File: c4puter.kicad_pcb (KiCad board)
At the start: 6 copper layers, 200 x 200 mm, 181 parts, among them J1 PDI, J7 19V 3A, J8 DEBUG, Q1 AOD4189, Q2 AOD4189, Q3 2N7002, U1 ATXMEGA8E5-MU

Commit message: MOAR WORK
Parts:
- added C9: 100n, IPC7351-Nominal:CAPC1005X55, F.Cu at (90.5, 1.96)
- added J2: MICROSD, manuf:AMPHENOL-114-00841-68, F.Cu at (100.0, 4.00)
- added R56: 100k, IPC7351-Nominal:RESC1608X50, F.Cu at (90.5, 3.77)
- LIMB1: value LPC435xFET256 -> ATSAM4S16CA-AU; footprint smd-semi:BGA100P1700X1700-256 -> IPC7351-Nominal:QFP50P1600X1600X160-100
- moved LIMB1 1.00 mm to (78.0, 21.0), turned to 90 degrees
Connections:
- DZ1 pad 2: /EC/USB0_D- -> /EC/USB_D-
- DZ1 pad 3: /EC/USB0_D+ -> /EC/USB_D+
- J8 pad 2: /EC/USB0_D+ -> /EC/USB_D+
- J8 pad 3: /EC/USB0_D- -> /EC/USB_D-
- R4 pad 1: /EC/USB0_VBUS -> /EC/USB_VBUS
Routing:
- net /EC/USB0_D-: track 66.9 -> 0.00 mm
- net /EC/USB0_D+: track 66.0 -> 0.00 mm
- net /EC/USB_D-: track 0.00 -> 40.1 mm
- net /EC/USB_D+: track 0.00 -> 39.8 mm
- net /EC/USB0_VBUS: track 28.7 -> 0.00 mm
- net GND: track 84.2 -> 68.6 mm, vias 94 -> 72
- net 3V3_LIMB: track 17.1 -> 2.29 mm, vias 22 -> 1

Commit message: MOAR WORK, v2
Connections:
- net /EC/NCS0 renamed /Multibridge/LIMBNCS
- net /EC/NRD renamed /Multibridge/LIMBNRD
- net /EC/NWAIT renamed /Multibridge/LIMBNWAIT
- net /EC/NWE renamed /Multibridge/LIMBNWE
- BRIDGE1 pad AA15: VRAM -> VCCO_2
- BRIDGE1 pad AA19: VRAM -> VCCO_2
- BRIDGE1 pad AA3: VRAM -> VCCO_2
- BRIDGE1 pad AA7: VRAM -> VCCO_2
- BRIDGE1 pad AB10: VDDRREF -> Net-(BRIDGE1-PadAB10)
- BRIDGE1 pad AB14: VDDRREF -> Net-(BRIDGE1-PadAB14)
- BRIDGE1 pad AB7: VDDRREF -> Net-(BRIDGE1-PadAB7)
- BRIDGE1 pad B20: Net-(BRIDGE1-PadB20) -> VDDRREF
- BRIDGE1 pad C20: Net-(BRIDGE1-PadC20) -> /Multibridge/DM1
- BRIDGE1 pad C21: VCCO1 -> VRAM
- BRIDGE1 pad D19: Net-(BRIDGE1-PadD19) -> /Multibridge/DQ1
- BRIDGE1 pad E19: VCCO1 -> VRAM
- BRIDGE1 pad E20: Net-(BRIDGE1-PadE20) -> /Multibridge/DQ14
- BRIDGE1 pad F20: Net-(BRIDGE1-PadF20) -> /Multibridge/DQ4
- BRIDGE1 pad G21: VCCO1 -> VRAM
- BRIDGE1 pad H18: Net-(BRIDGE1-PadH18) -> /Multibridge/DQ3
- BRIDGE1 pad H19: Net-(BRIDGE1-PadH19) -> /Multibridge/DQ2
- BRIDGE1 pad J17: Net-(BRIDGE1-PadJ17) -> /Multibridge/DM0
- BRIDGE1 pad J18: VCCO1 -> VRAM
- BRIDGE1 pad K17: Net-(BRIDGE1-PadK17) -> /Multibridge/DQ0
- BRIDGE1 pad L16: VCCO1 -> VRAM
- BRIDGE1 pad L21: VCCO1 -> VRAM
- BRIDGE1 pad N18: VCCO1 -> VRAM
- BRIDGE1 pad N19: Net-(BRIDGE1-PadN19) -> VDDRREF
- BRIDGE1 pad R21: VCCO1 -> VRAM
- BRIDGE1 pad R7: /Multibridge/DQ3 -> Net-(BRIDGE1-PadR7)
- BRIDGE1 pad R8: /Multibridge/DQ4 -> Net-(BRIDGE1-PadR8)
- BRIDGE1 pad T13: VRAM -> VCCO_2
- BRIDGE1 pad T7: /Multibridge/DQ2 -> Net-(BRIDGE1-PadT7)
- BRIDGE1 pad T9: VRAM -> VCCO_2
- BRIDGE1 pad U18: VCCO1 -> VRAM
- BRIDGE1 pad U6: /Multibridge/DM0 -> Net-(BRIDGE1-PadU6)
- BRIDGE1 pad V12: VRAM -> VCCO_2
- BRIDGE1 pad V16: VRAM -> VCCO_2
- BRIDGE1 pad V5: /Multibridge/DQ0 -> Net-(BRIDGE1-PadV5)
- BRIDGE1 pad V8: VRAM -> VCCO_2
- BRIDGE1 pad W21: VCCO1 -> VRAM
- BRIDGE1 pad W4: /Multibridge/DQ14 -> Net-(BRIDGE1-PadW4)
- BRIDGE1 pad W5: VRAM -> VCCO_2
- BRIDGE1 pad W6: /Multibridge/DQ1 -> Net-(BRIDGE1-PadW6)
- BRIDGE1 pad Y3: /Multibridge/DM1 -> Net-(BRIDGE1-PadY3)
- PCI1 pad A17: /PerBus/PCI_GNT#0 -> /PerBus/PCI_GNT#1
- PCI1 pad B18: /PerBus/PCI_REQ#0 -> /PerBus/PCI_REQ#1
- PCI2 pad A17: /PerBus/PCI_GNT#0 -> /PerBus/PCI_GNT#2
- PCI2 pad B18: /PerBus/PCI_REQ#0 -> /PerBus/PCI_REQ#2
- PCI3 pad A17: /PerBus/PCI_GNT#0 -> /PerBus/PCI_GNT#3
- PCI3 pad B18: /PerBus/PCI_REQ#0 -> /PerBus/PCI_REQ#3
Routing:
- net /PerBus/PCI_INTB#: track 78.2 -> 0.00 mm, vias 1 -> 0
- net /PerBus/PCI_INTD#: track 76.7 -> 0.00 mm
- net /PerBus/PCI_INTA#: track 74.3 -> 0.00 mm, vias 1 -> 0
- net /PerBus/PCI_INTC#: track 70.7 -> 0.00 mm, vias 1 -> 0
- net /PerBus/PCI_CLK: track 65.9 -> 0.00 mm
- net /Multibridge/DM1: track 54.5 -> 1.63 mm, vias 2 -> 1
- net /Multibridge/DQ14: track 54.1 -> 2.31 mm
- net /Multibridge/DQ1: track 51.9 -> 1.69 mm, vias 2 -> 1
- net /Multibridge/DQ2: track 50.5 -> 1.67 mm, vias 2 -> 1
- net /Multibridge/DQ3: track 49.8 -> 1.69 mm, vias 2 -> 1
- net /Multibridge/DQ0: track 50.3 -> 2.38 mm
- net /Multibridge/DM0: track 50.2 -> 2.40 mm
- net /Multibridge/DQ4: track 60.7 -> 38.2 mm, vias 2 -> 1
- net VCCO_2: track 0.00 -> 7.07 mm, vias 0 -> 10
- net VCCO1: track 7.07 -> 0.00 mm, vias 10 -> 0
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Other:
- net class Default: via_dia 0.8 -> 0.5; via_drill 0.4 -> 0.2

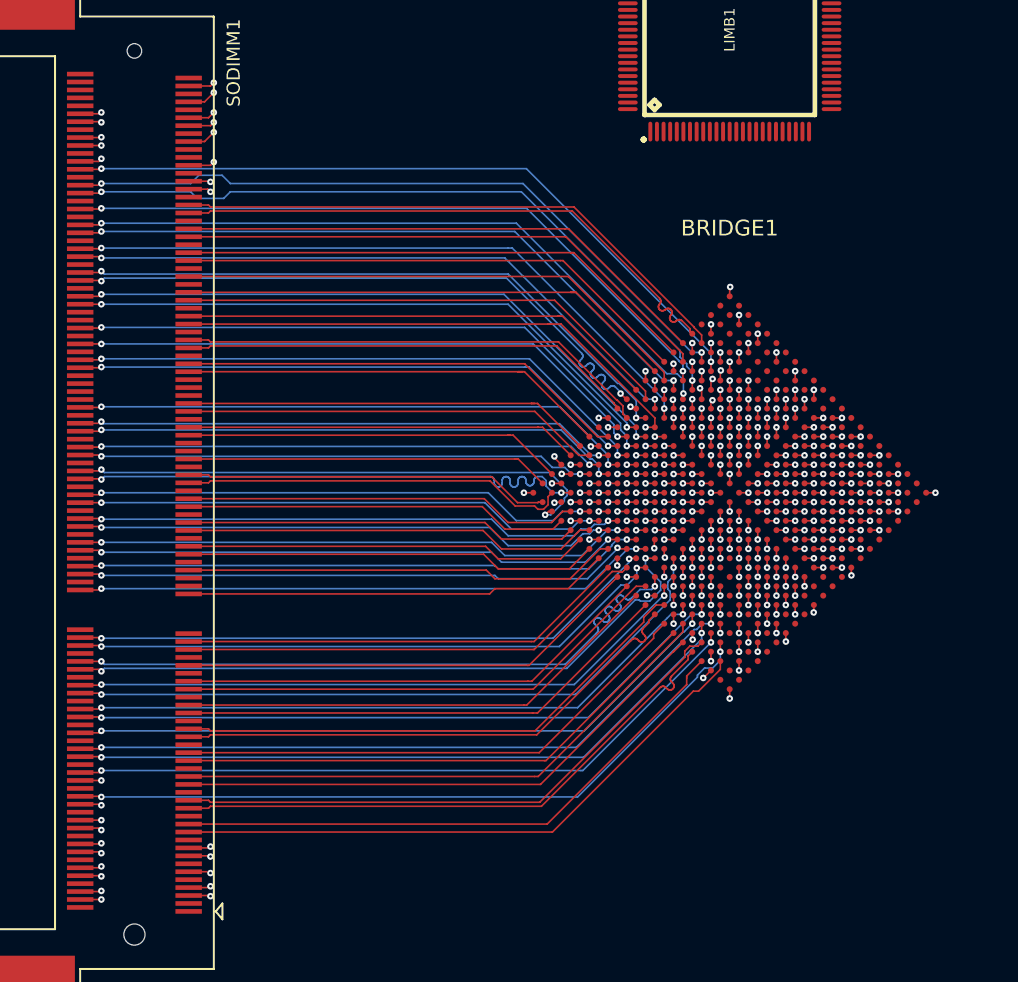
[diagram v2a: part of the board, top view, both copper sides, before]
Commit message: Rip up SDRAM and rotate FPGA
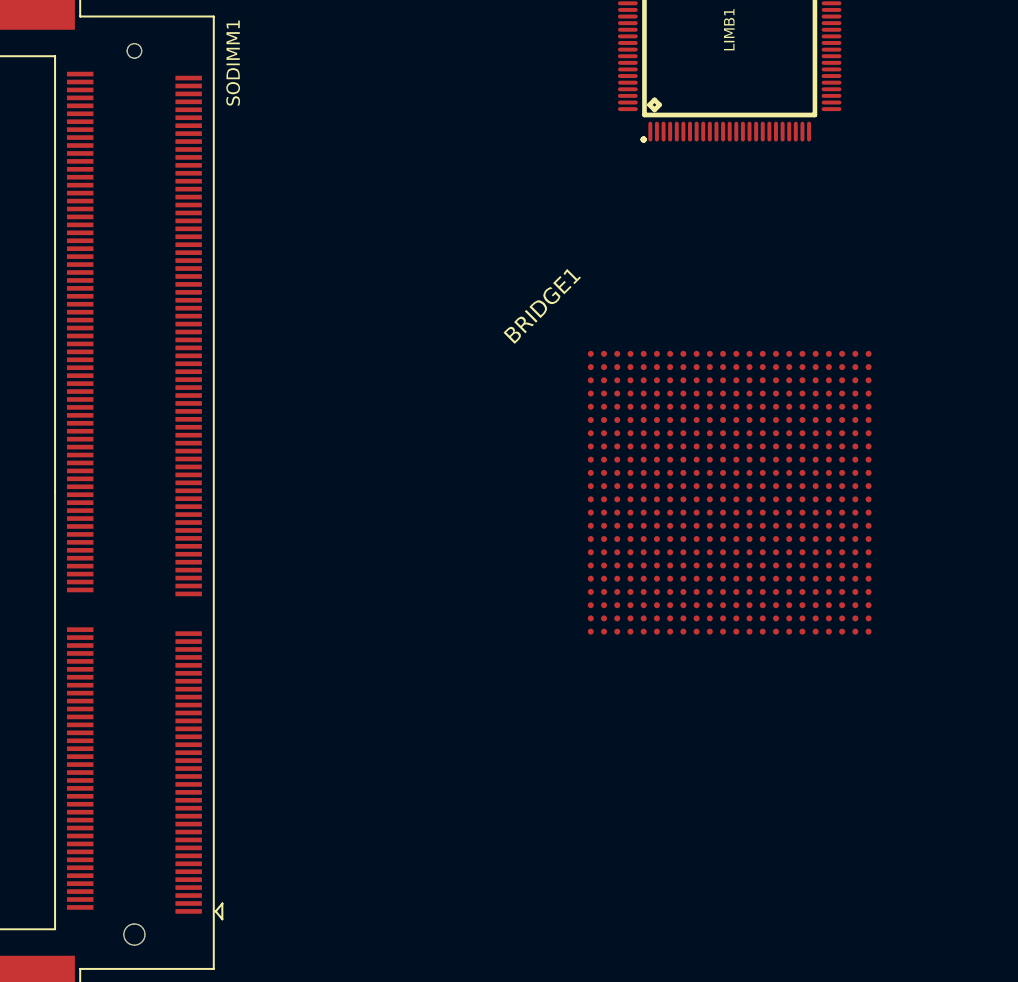
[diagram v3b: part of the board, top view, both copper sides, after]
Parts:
- turned BRIDGE1 to 90 degrees
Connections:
- net Net-(SODIMM1-Pad1) renamed /Power Distrib/VREFDQ
- net Net-(SODIMM1-Pad199) renamed /Power Distrib/VDDSPD
- BRIDGE1 pad A10: /Multibridge/DQS4_N -> Net-(BRIDGE1-PadA10)
- BRIDGE1 pad A11: /Multibridge/DQS5_N -> Net-(BRIDGE1-PadA11)
- BRIDGE1 pad A12: /Multibridge/DQ35 -> Net-(BRIDGE1-PadA12)
- BRIDGE1 pad A14: /Multibridge/DQ41 -> Net-(BRIDGE1-PadA14)
- BRIDGE1 pad A15: /Multibridge/DQ42 -> Net-(BRIDGE1-PadA15)
- BRIDGE1 pad A16: /Multibridge/DQ43 -> Net-(BRIDGE1-PadA16)
- BRIDGE1 pad A17: /Multibridge/DQ49 -> Net-(BRIDGE1-PadA17)
- BRIDGE1 pad A18: /Multibridge/DQS6_N -> Net-(BRIDGE1-PadA18)
- BRIDGE1 pad A2: /Multibridge/A10 -> Net-(BRIDGE1-PadA2)
- BRIDGE1 pad A3: /Multibridge/~WE -> Net-(BRIDGE1-PadA3)
- BRIDGE1 pad A5: /Multibridge/~CAS -> Net-(BRIDGE1-PadA5)
- BRIDGE1 pad A6: /Multibridge/~S1 -> Net-(BRIDGE1-PadA6)
- BRIDGE1 pad A7: /Multibridge/DQ32 -> Net-(BRIDGE1-PadA7)
- BRIDGE1 pad B1: /Multibridge/CK0_N -> Net-(BRIDGE1-PadB1)
- BRIDGE1 pad B10: /Multibridge/DQS4_P -> Net-(BRIDGE1-PadB10)
- BRIDGE1 pad B12: /Multibridge/DQ40 -> Net-(BRIDGE1-PadB12)
- BRIDGE1 pad B14: /Multibridge/DM5 -> Net-(BRIDGE1-PadB14)
- BRIDGE1 pad B16: /Multibridge/DQ48 -> Net-(BRIDGE1-PadB16)
- BRIDGE1 pad B18: /Multibridge/DQS6_P -> Net-(BRIDGE1-PadB18)
- BRIDGE1 pad B2: /Multibridge/CK0_P -> Net-(BRIDGE1-PadB2)
- BRIDGE1 pad B6: /Multibridge/A13 -> Net-(BRIDGE1-PadB6)
- BRIDGE1 pad B8: /Multibridge/DQ33 -> Net-(BRIDGE1-PadB8)
- BRIDGE1 pad C1: /Multibridge/CK1_N -> Net-(BRIDGE1-PadC1)
- BRIDGE1 pad C10: /Multibridge/DQ44 -> Net-(BRIDGE1-PadC10)
- BRIDGE1 pad C11: /Multibridge/DQS5_P -> Net-(BRIDGE1-PadC11)
- BRIDGE1 pad C12: /Multibridge/DQ46 -> Net-(BRIDGE1-PadC12)
- BRIDGE1 pad C14: /Multibridge/DQ52 -> Net-(BRIDGE1-PadC14)
- BRIDGE1 pad C15: /Multibridge/DM6 -> Net-(BRIDGE1-PadC15)
- BRIDGE1 pad C17: /Multibridge/DQ55 -> Net-(BRIDGE1-PadC17)
- BRIDGE1 pad C20: /Multibridge/DM1 -> Net-(BRIDGE1-PadC20)
- BRIDGE1 pad C3: /Multibridge/CK1_P -> Net-(BRIDGE1-PadC3)
- BRIDGE1 pad C5: /Multibridge/BA1 -> Net-(BRIDGE1-PadC5)
- BRIDGE1 pad C6: /Multibridge/~RAS -> Net-(BRIDGE1-PadC6)
- BRIDGE1 pad C7: /Multibridge/ODT0 -> Net-(BRIDGE1-PadC7)
- BRIDGE1 pad C8: /Multibridge/DQ36 -> Net-(BRIDGE1-PadC8)
- BRIDGE1 pad C9: /Multibridge/DM4 -> Net-(BRIDGE1-PadC9)
- BRIDGE1 pad D1: /Multibridge/A3 -> Net-(BRIDGE1-PadD1)
- BRIDGE1 pad D10: /Multibridge/DQ45 -> Net-(BRIDGE1-PadD10)
- BRIDGE1 pad D11: /Multibridge/DQ34 -> Net-(BRIDGE1-PadD11)
- BRIDGE1 pad D12: /Multibridge/DQ47 -> Net-(BRIDGE1-PadD12)
- BRIDGE1 pad D13: /Multibridge/DQS7_N -> Net-(BRIDGE1-PadD13)
- BRIDGE1 pad D14: /Multibridge/DQ53 -> Net-(BRIDGE1-PadD14)
- BRIDGE1 pad D15: /Multibridge/DQ54 -> Net-(BRIDGE1-PadD15)
- BRIDGE1 pad D17: /Multibridge/DQ60 -> Net-(BRIDGE1-PadD17)
- BRIDGE1 pad D19: /Multibridge/DQ1 -> Net-(BRIDGE1-PadD19)
- BRIDGE1 pad D2: /Multibridge/A1 -> Net-(BRIDGE1-PadD2)
- BRIDGE1 pad D6: /Multibridge/~S0 -> Net-(BRIDGE1-PadD6)
- BRIDGE1 pad D7: /Multibridge/ODT1 -> Net-(BRIDGE1-PadD7)
- BRIDGE1 pad D8: /Multibridge/DQ37 -> Net-(BRIDGE1-PadD8)
- BRIDGE1 pad D9: /Multibridge/DQ38 -> Net-(BRIDGE1-PadD9)
- BRIDGE1 pad E1: /Multibridge/A5 -> Net-(BRIDGE1-PadE1)
- BRIDGE1 pad E14: /Multibridge/DM7 -> Net-(BRIDGE1-PadE14)
- BRIDGE1 pad E16: /Multibridge/DQ63 -> Net-(BRIDGE1-PadE16)
- BRIDGE1 pad E20: /Multibridge/DQ14 -> Net-(BRIDGE1-PadE20)
- BRIDGE1 pad E3: /Multibridge/A0 -> Net-(BRIDGE1-PadE3)
- BRIDGE1 pad F1: /Multibridge/A9 -> Net-(BRIDGE1-PadF1)
- BRIDGE1 pad F12: /Multibridge/DQ61 -> Net-(BRIDGE1-PadF12)
- BRIDGE1 pad F13: /Multibridge/DQS7_P -> Net-(BRIDGE1-PadF13)
- BRIDGE1 pad F14: /Multibridge/DQ59 -> Net-(BRIDGE1-PadF14)
- BRIDGE1 pad F15: /Multibridge/SA0 -> Net-(BRIDGE1-PadF15)
- BRIDGE1 pad F2: /Multibridge/A8 -> Net-(BRIDGE1-PadF2)
- BRIDGE1 pad F20: /Multibridge/DQ4 -> Net-(BRIDGE1-PadF20)
- BRIDGE1 pad F3: /Multibridge/A2 -> Net-(BRIDGE1-PadF3)
- BRIDGE1 pad F5: /Multibridge/DQ50 -> Net-(BRIDGE1-PadF5)
- BRIDGE1 pad G1: /Multibridge/A12 -> Net-(BRIDGE1-PadG1)
- BRIDGE1 pad G13: /Multibridge/DQ58 -> Net-(BRIDGE1-PadG13)
- BRIDGE1 pad G3: /Multibridge/A6 -> Net-(BRIDGE1-PadG3)
- BRIDGE1 pad G4: /Multibridge/A4 -> Net-(BRIDGE1-PadG4)
- BRIDGE1 pad G6: /Multibridge/DQ51 -> Net-(BRIDGE1-PadG6)
- BRIDGE1 pad H1: /Multibridge/CKE0 -> Net-(BRIDGE1-PadH1)
- BRIDGE1 pad H12: /Multibridge/DQ56 -> Net-(BRIDGE1-PadH12)
- BRIDGE1 pad H13: /Multibridge/DQ62 -> Net-(BRIDGE1-PadH13)
- BRIDGE1 pad H14: /Multibridge/SA1 -> Net-(BRIDGE1-PadH14)
- BRIDGE1 pad H18: /Multibridge/DQ3 -> Net-(BRIDGE1-PadH18)
- BRIDGE1 pad H19: /Multibridge/DQ2 -> Net-(BRIDGE1-PadH19)
- BRIDGE1 pad H2: /Multibridge/BA2 -> Net-(BRIDGE1-PadH2)
- BRIDGE1 pad H3: /Multibridge/A11 -> Net-(BRIDGE1-PadH3)
- BRIDGE1 pad H4: /Multibridge/A7 -> Net-(BRIDGE1-PadH4)
- BRIDGE1 pad H5: /Multibridge/DQ7 -> Net-(BRIDGE1-PadH5)
- BRIDGE1 pad H6: /Multibridge/DQ12 -> Net-(BRIDGE1-PadH6)
- BRIDGE1 pad H8: /Multibridge/DQ13 -> Net-(BRIDGE1-PadH8)
- BRIDGE1 pad J1: /Multibridge/DQ27 -> Net-(BRIDGE1-PadJ1)
- BRIDGE1 pad J17: /Multibridge/DM0 -> Net-(BRIDGE1-PadJ17)
- BRIDGE1 pad J3: /Multibridge/A15 -> Net-(BRIDGE1-PadJ3)
- BRIDGE1 pad J4: /Multibridge/A14 -> Net-(BRIDGE1-PadJ4)
- BRIDGE1 pad J6: /Multibridge/DQS0_N -> Net-(BRIDGE1-PadJ6)
- BRIDGE1 pad J7: /Multibridge/DQ6 -> Net-(BRIDGE1-PadJ7)
- BRIDGE1 pad K1: /Multibridge/DM3 -> Net-(BRIDGE1-PadK1)
- BRIDGE1 pad K17: /Multibridge/DQ0 -> Net-(BRIDGE1-PadK17)
- BRIDGE1 pad K2: /Multibridge/DQ26 -> Net-(BRIDGE1-PadK2)
- BRIDGE1 pad K3: /Multibridge/DQ31 -> Net-(BRIDGE1-PadK3)
- BRIDGE1 pad K4: /Multibridge/CKE1 -> Net-(BRIDGE1-PadK4)
- BRIDGE1 pad K5: /Multibridge/DQ5 -> Net-(BRIDGE1-PadK5)
- BRIDGE1 pad K6: /Multibridge/DQS0_P -> Net-(BRIDGE1-PadK6)
- BRIDGE1 pad L1: /Multibridge/DQ25 -> Net-(BRIDGE1-PadL1)
- BRIDGE1 pad L3: /Multibridge/DQ30 -> Net-(BRIDGE1-PadL3)
- BRIDGE1 pad L4: /Multibridge/DQS3_N -> Net-(BRIDGE1-PadL4)
- BRIDGE1 pad M1: /Multibridge/DQ19 -> Net-(BRIDGE1-PadM1)
- BRIDGE1 pad M2: /Multibridge/DQ24 -> Net-(BRIDGE1-PadM2)
- BRIDGE1 pad M3: /Multibridge/DQS3_P -> Net-(BRIDGE1-PadM3)
- BRIDGE1 pad M5: /Multibridge/DQ28 -> Net-(BRIDGE1-PadM5)
- BRIDGE1 pad N1: /Multibridge/DQ18 -> Net-(BRIDGE1-PadN1)
- BRIDGE1 pad N3: /Multibridge/DQ29 -> Net-(BRIDGE1-PadN3)
- BRIDGE1 pad P1: /Multibridge/DQS2_N -> Net-(BRIDGE1-PadP1)
- BRIDGE1 pad P2: /Multibridge/DQS2_P -> Net-(BRIDGE1-PadP2)
- BRIDGE1 pad R1: /Multibridge/DQ17 -> Net-(BRIDGE1-PadR1)
- BRIDGE1 pad R3: /Multibridge/DQ23 -> Net-(BRIDGE1-PadR3)
- BRIDGE1 pad T1: /Multibridge/DQ16 -> Net-(BRIDGE1-PadT1)
- BRIDGE1 pad T2: /Multibridge/DQ11 -> Net-(BRIDGE1-PadT2)
- BRIDGE1 pad T3: /Multibridge/DM2 -> Net-(BRIDGE1-PadT3)
- BRIDGE1 pad T4: /Multibridge/DQ22 -> Net-(BRIDGE1-PadT4)
- BRIDGE1 pad U1: /Multibridge/DQ10 -> Net-(BRIDGE1-PadU1)
- BRIDGE1 pad U3: /Multibridge/DQ20 -> Net-(BRIDGE1-PadU3)
- BRIDGE1 pad U4: /Multibridge/DQ21 -> Net-(BRIDGE1-PadU4)
- BRIDGE1 pad V1: /Multibridge/DQS1_N -> Net-(BRIDGE1-PadV1)
- BRIDGE1 pad V2: /Multibridge/DQS1_P -> Net-(BRIDGE1-PadV2)
- BRIDGE1 pad V3: /Multibridge/DQ15 -> Net-(BRIDGE1-PadV3)
- BRIDGE1 pad W1: /Multibridge/DQ9 -> Net-(BRIDGE1-PadW1)
- BRIDGE1 pad W3: /Multibridge/SDRAM_~RST -> Net-(BRIDGE1-PadW3)
- BRIDGE1 pad Y2: /Multibridge/DQ8 -> Net-(BRIDGE1-PadY2)
- SODIMM1 pad 106: (no net) -> +1.5
- SODIMM1 pad 109: (no net) -> /Multibridge/BA0
- SODIMM1 pad 112: (no net) -> +1.5
- SODIMM1 pad 118: (no net) -> +1.5
- SODIMM1 pad 122: (no net) -> Net-(SODIMM1-Pad122)
- SODIMM1 pad 124: (no net) -> +1.5
- SODIMM1 pad 125: (no net) -> Net-(SODIMM1-Pad125)
- SODIMM1 pad 126: (no net) -> /Power Distrib/VREFCA
- SODIMM1 pad 128: (no net) -> GND
- SODIMM1 pad 134: (no net) -> GND
- SODIMM1 pad 138: (no net) -> GND
- SODIMM1 pad 144: (no net) -> GND
- SODIMM1 pad 150: (no net) -> GND
- SODIMM1 pad 156: (no net) -> GND
- SODIMM1 pad 198: (no net) -> /Power Distrib/~EVENT
- SODIMM1 pad 203: Net-(SODIMM1-Pad203) -> /Power Distrib/VTT
- SODIMM1 pad 204: Net-(SODIMM1-Pad204) -> /Power Distrib/VTT
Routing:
- net /Multibridge/DQ62: track 62.6 -> 0.00 mm, vias 2 -> 0
- net /Multibridge/DQ63: track 59.6 -> 0.00 mm, vias 2 -> 0
- net /Multibridge/SA1: track 58.0 -> 0.00 mm, vias 2 -> 0
- net /Multibridge/DQ61: track 57.7 -> 0.00 mm, vias 2 -> 0
- net /Multibridge/DQS0_P: track 57.3 -> 0.00 mm, vias 2 -> 0
- net /Multibridge/DQS0_N: track 57.2 -> 0.00 mm, vias 2 -> 0
- net /Multibridge/DQS7_N: track 56.4 -> 0.00 mm, vias 2 -> 0
- net /Multibridge/DQS7_P: track 56.4 -> 0.00 mm, vias 2 -> 0
- net /Multibridge/DQ5: track 55.4 -> 0.00 mm, vias 2 -> 0
- net /Multibridge/DQ6: track 54.9 -> 0.00 mm, vias 2 -> 0
- net /Multibridge/DQ60: track 54.8 -> 0.00 mm, vias 2 -> 0
- net /Multibridge/DQ13: track 54.7 -> 0.00 mm, vias 2 -> 0
- net /Multibridge/SA0: track 54.2 -> 0.00 mm, vias 2 -> 0
- net /Multibridge/SDRAM_~RST: track 54.1 -> 0.00 mm, vias 2 -> 0
- net /Multibridge/DQ54: track 54.1 -> 0.00 mm, vias 2 -> 0
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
